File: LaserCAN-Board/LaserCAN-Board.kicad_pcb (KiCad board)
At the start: 4 copper layers, 25 x 25 mm, 35 parts, among them J2 TC2050-IDC-NL, U2 VL53L1CXV0FY1, U3 M24C64-RMN6TP, U4 STM32F103C8Tx, U5 MCP1703Ax-330xxTT, U6 SN65HVD230

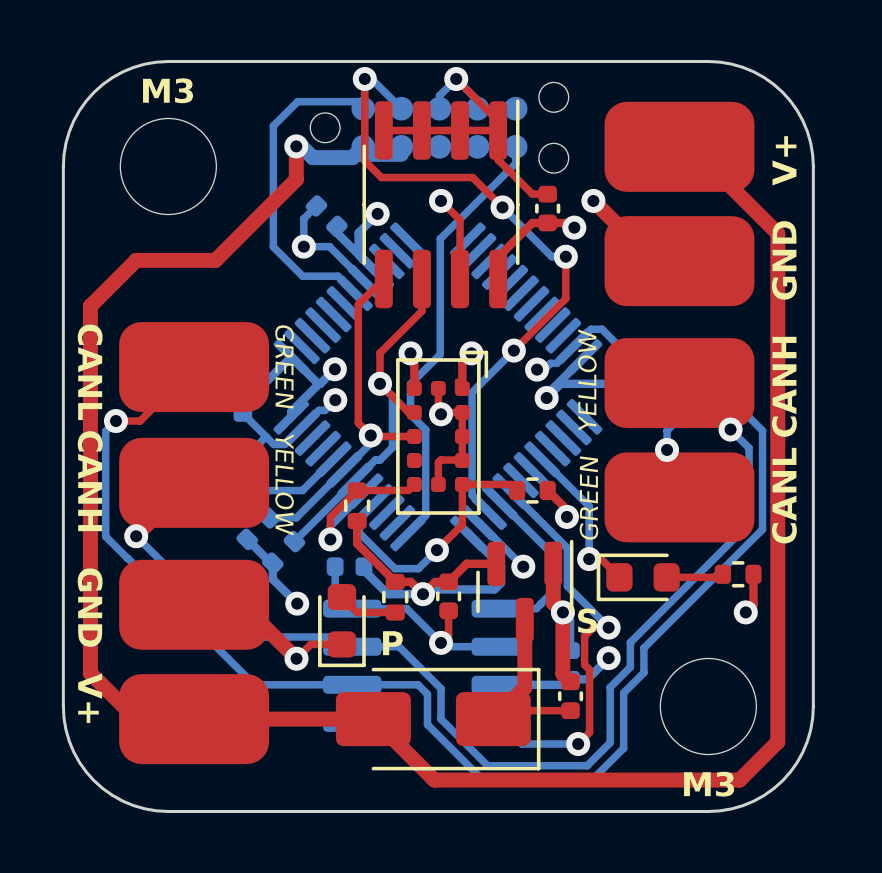
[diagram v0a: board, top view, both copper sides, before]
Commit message: Update to v3.1 - Improved voltage regulation performance, improved ESD protection
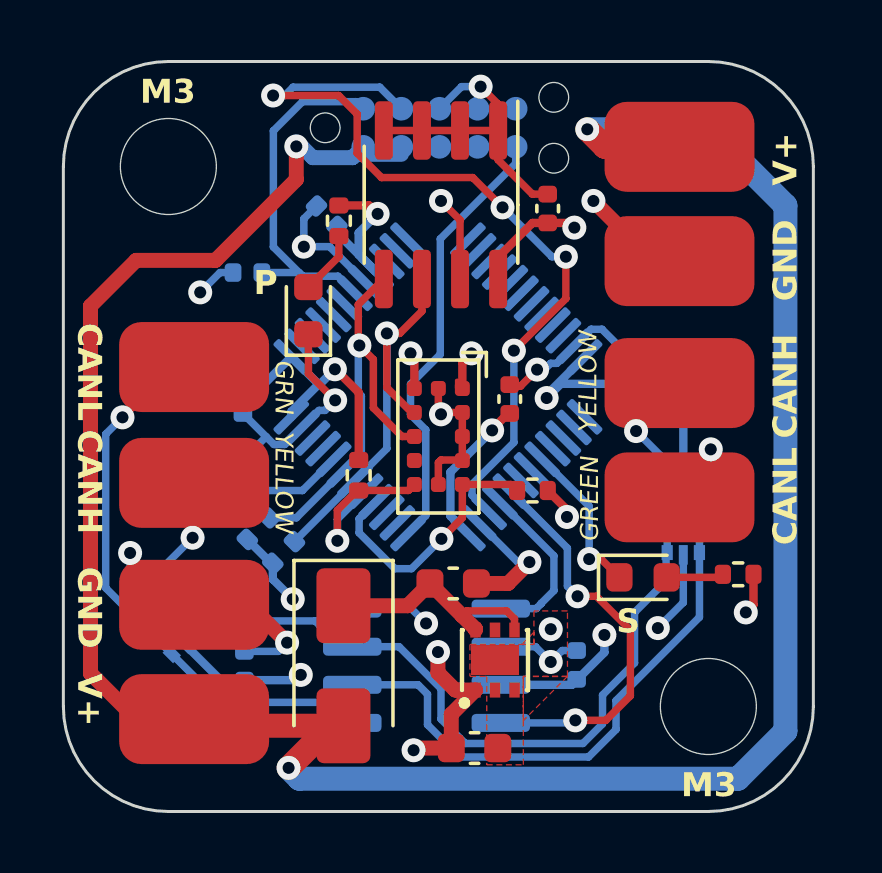
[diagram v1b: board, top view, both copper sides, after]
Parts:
- added C10: 100n, Capacitor_SMD:C_0402_1005Metric, B.Cu at (126.0, 120.1)
- added C11: 100n, Capacitor_SMD:C_0402_1005Metric, B.Cu at (140.6, 110.2)
- added C3: 10uF, Capacitor_SMD:C_0603_1608Metric, F.Cu at (133.7, 122.9)
- added U1: NCP730BMT330TBG, NCP730BMT330TBG:WDFN-6_L2.0-W2.0-P0.65-BL-EP-1, F.Cu at (134.4, 120.0)
- added U7: USBLC6-2P6, Package_TO_SOT_SMD:SOT-666, B.Cu at (140.7, 115.5)
- C1: value 1uF -> 10uF; footprint Capacitor_SMD:C_0402_1005Metric -> Capacitor_SMD:C_0603_1608Metric
- C4: value 1uF -> 100n; moved to B.Cu
- C8: moved to F.Cu
- U5: value MCP1703Ax-330xxTT -> USBLC6-2P6; footprint Package_TO_SOT_SMD:SOT-23 -> Package_TO_SOT_SMD:SOT-666; moved to B.Cu
- moved C4 12.7 mm to (126.1, 107.0), turned to 0 degrees
- moved R7 12.7 mm to (129.2, 105.3)
- moved U5 12.0 mm to (123.4, 118.8), turned to -45 degrees
- moved D3 10.4 mm to (128.2, 108.3)
- moved C8 7.73 mm to (134.9, 111.3), turned to 90 degrees
- moved C1 5.43 mm to (133.0, 117.4), turned to 0 degrees
- moved D1 3.48 mm to (129.3, 120.1), turned to -90 degrees
- moved R5 1.02 mm to (129.8, 113.8), turned to -90 degrees
- moved C9 0.20 mm to (137.1, 120.1)
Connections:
- C4 pad 1: +3V3 -> GND
- C4 pad 2: GND -> /NRST
- U5 pad 1: GND -> /CANL
- U5 pad 2: +3V3 -> GND
- U5 pad 3: Net-(D1-K) -> /CANH
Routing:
- net +3V3: track 44.7 -> 56.4 mm, vias 11 -> 14
- net +12V: track 72.3 -> 83.3 mm, vias 1 -> 3
- net /CANL: track 47.7 -> 42.5 mm
- net /SWDIO: track 22.4 -> 27.5 mm
- net GND: track 58.5 -> 62.4 mm, vias 11 -> 15
- net /I2C_SDA: track 11.9 -> 14.2 mm
- net /CANH: track 37.5 -> 35.4 mm
- net /I2C_SCL: track 12.5 -> 13.8 mm
- net /NRST: track 10.8 -> 12.1 mm
- net Net-(D1-K): track 6.42 -> 7.67 mm
- added copper zone on F.Cu, net GND
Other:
- board text added: "GRN"
- board text added: "LaserCAN Rev. 3.1"
- board text removed: "LaserCAN Rev. 3"

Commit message: Update to new power regulation circuitry
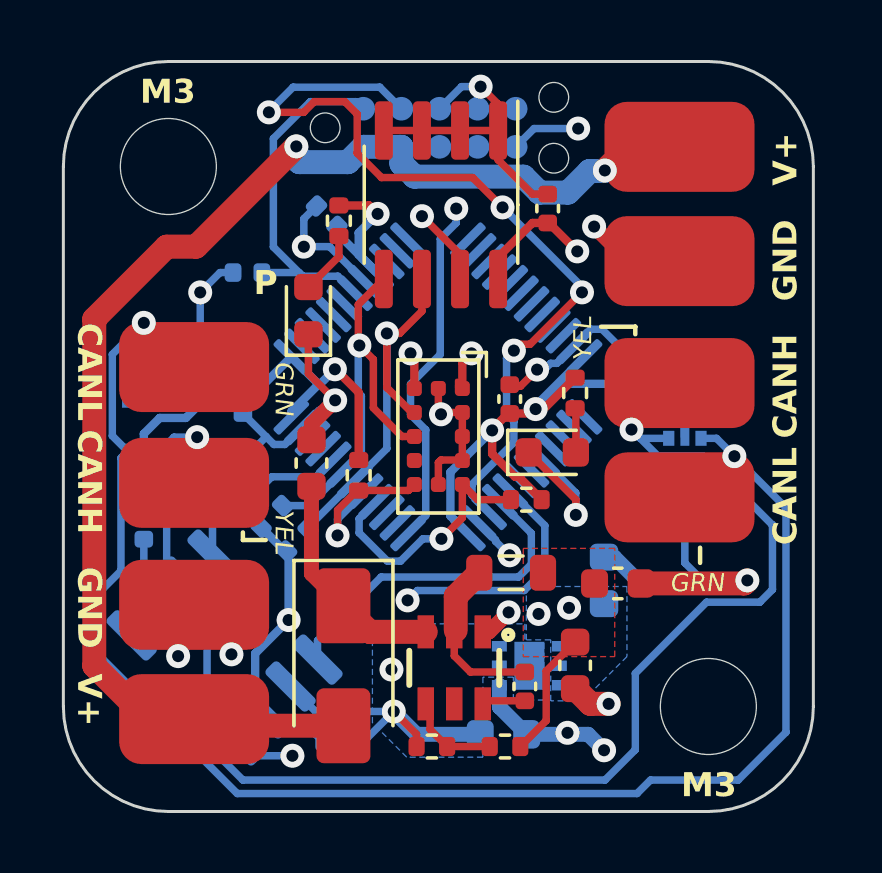
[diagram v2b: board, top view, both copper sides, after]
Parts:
- added C12: 10uF, Capacitor_SMD:C_0603_1608Metric, F.Cu at (128.3, 113.4)
- added C13: 10uF, Capacitor_SMD:C_0603_1608Metric, F.Cu at (138.5, 117.4)
- added C14: 100n, Capacitor_SMD:C_0402_1005Metric, F.Cu at (135.4, 120.8)
- added C15: 10uF, Capacitor_SMD:C_0603_1608Metric, F.Cu at (137.1, 120.1)
- added L1: 4.7uH, Inductor_SMD:L_0805_2012Metric, F.Cu at (134.9, 117.0)
- added R2: 41k 1%, Resistor_SMD:R_0402_1005Metric, F.Cu at (134.7, 122.8)
- added R8: 10k 1%, Resistor_SMD:R_0402_1005Metric, F.Cu at (132.3, 122.8)
- added U8: AP62200TWU-7, AP62200TWU-7:TSOT-26_L2.9-W1.6-P0.95-LS2.8-BL, F.Cu at (133.0, 120.2)
- C1, C3, U1: moved to B.Cu
- moved C9 8.35 mm to (129.2, 122.7), turned to 180 degrees
- moved R6 8.13 mm to (137.1, 111.0), turned to -90 degrees
- moved U6 6.76 mm to (125.4, 119.5), turned to 135 degrees
- moved U5 6.67 mm to (122.7, 112.1), turned to -90 degrees
- moved C10 5.77 mm to (122.7, 115.4), turned to -90 degrees
- moved D2 5.15 mm to (136.3, 113.0)
- moved C1 5.03 mm to (138.0, 117.3), turned to 90 degrees
- moved U7 2.11 mm to (140.7, 113.4)
- moved U1 1.16 mm to (135.5, 120.1), turned to 90 degrees
- moved C3 1.07 mm to (134.7, 122.4), turned to 180 degrees
- moved R3 0.61 mm to (127.8, 116.0)
- moved R4 0.61 mm to (126.9, 115.2)
- moved R1 0.37 mm to (135.4, 114.6)
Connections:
- C1 pad 1: Net-(D1-K) -> +3V9
- U1 pad 4: Net-(D1-K) -> +3V9
- U1 pad 6: Net-(D1-K) -> +3V9
- U5 pad 1: /CANL -> unconnected-(U5-I/O1-Pad1)
- U5 pad 3: /CANH -> unconnected-(U5-I/O2-Pad3)
- U7 pad 1: /CANL -> unconnected-(U7-I/O1-Pad1)
- U7 pad 3: /CANH -> unconnected-(U7-I/O2-Pad3)
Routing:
- net +12V: track 83.3 -> 44.8 mm, vias 3 -> 2
- net GND: track 62.4 -> 86.1 mm, vias 15 -> 16
- net /CANH: track 35.4 -> 45.2 mm
- net /CANL: track 42.5 -> 50.9 mm
- net +3V3: track 56.4 -> 62.7 mm, vias 14 -> 10
- net Net-(U8-SW): track 0.00 -> 5.62 mm
- net /CAN_TX: track 5.74 -> 11.3 mm
- net /SWCLK: track 14.8 -> 19.4 mm, vias 0 -> 2
- net +3V9: track 0.00 -> 4.24 mm, vias 0 -> 2
- net /CAN_RX: track 13.5 -> 17.0 mm
- net Net-(U8-FB): track 0.00 -> 3.14 mm
- net Net-(U8-BST): track 0.00 -> 1.44 mm
- net /SWDIO: track 27.5 -> 28.6 mm
- net /I2C_SDA: track 14.2 -> 13.6 mm
- net /I2C_SCL: track 13.8 -> 13.2 mm
- added copper zone on B.Cu, net +3V9
- added copper zone on F.Cu, net +3V9
- added copper zone on B.Cu, net GND
- removed copper zone on F.Cu, net GND
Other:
- board text added: "YEL"
- board text removed: "GREEN"
- board text removed: "S"
- board text removed: "YELLOW"

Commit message: Updates
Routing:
- net GND: track 86.1 -> 88.0 mm
- net +12V: track 44.8 -> 45.8 mm
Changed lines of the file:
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@@
     (fp_line (start -0.399622 0.56) (end 0.399622 0.56)
       (stroke (width 0.12) (type solid)) (layer "F.SilkS"))
-    (fp_line (start -1.75 -0.85) (end 1.75 -0.85)
+    (fp_line (start -1.75 -1) (end 1.75 -1)
       (stroke (width 0.05) (type solid)) (layer "F.CrtYd"))
-    (fp_line (start -1.75 0.85) (end -1.75 -0.85)
+    (fp_line (start -1.75 1) (end -1.75 -1)
       (stroke (width 0.05) (type solid)) (layer "F.CrtYd"))
-    (fp_line (start 1.75 -0.85) (end 1.75 0.85)
+    (fp_line (start 1.75 -1) (end 1.75 1)
       (stroke (width 0.05) (type solid)) (layer "F.CrtYd"))
-    (fp_line (start 1.75 0.85) (end -1.75 0.85)
+    (fp_line (start 1.75 1) (end -1.75 1)
       (stroke (width 0.05) (type solid)) (layer "F.CrtYd"))
     (fp_line (start -1 -0.45) (end 1 -0.45)
@@
     (fp_line (start 1 0.45) (end -1 0.45)
       (stroke (width 0.1) (type solid)) (layer "F.Fab"))
-    (pad "1" smd roundrect (at -1.0625 0) (size 0.875 1.2) (layers "F.Cu" "F.Paste" "F.Mask") (roundrect_rratio 0.25)
+    (pad "1" smd roundrect (at -1.0625 0) (size 0.875 1.7) (layers "F.Cu" "F.Paste" "F.Mask") (roundrect_rratio 0.25)
       (net 55 "Net-(U8-SW)") (pintype "passive"))
-    (pad "2" smd roundrect (at 1.0625 0) (size 0.875 1.2) (layers "F.Cu" "F.Paste" "F.Mask") (roundrect_rratio 0.25)
+    (pad "2" smd roundrect (at 1.0625 0) (size 0.875 1.7) (layers "F.Cu" "F.Paste" "F.Mask") (roundrect_rratio 0.25)
       (net 54 "+3V9") (pintype "passive"))
     (model "${KICAD6_3DMODEL_DIR}/Inductor_SMD.3dshapes/L_0805_2012Metric.wrl"
@@
   (segment (start 132.5 111.672) (end 132.588 111.76) (width 0.25) (layer "F.Cu") (net 1))
   (segment (start 133.3 111.7) (end 132.648 111.7) (width 0.25) (layer "F.Cu") (net 1))
-  (via (at 134.874 116.459) (size 0.8) (drill 0.4) (layers "F.Cu" "B.Cu") (net 1))
+  (via (at 134.8745 116.205) (size 0.8) (drill 0.4) (layers "F.Cu" "B.Cu") (net 1))
   (via (at 131.0132 121.666) (size 0.8) (drill 0.4) (layers "F.Cu" "B.Cu") (net 1))
   (via (at 131.953 105.156) (size 0.8) (drill 0.4) (layers "F.Cu" "B.Cu") (net 1))
@@
   (segment (start 142.748 117.348) (end 142.7988 117.2972) (width 0.5) (layer "B.Cu") (net 1))
   (segment (start 124.5616 108.7489) (end 124.5616 107.696) (width 0.25) (layer "B.Cu") (net 1))
-  (segment (start 134.40668 115.94786) (end 133.838742 115.379922) (width 0.25) (layer "B.Cu") (net 1))
-  (segment (start 134.40668 115.99168) (end 134.40668 115.94786) (width 0.25) (layer "B.Cu") (net 1))
+  (segment (start 134.841079 118.362267) (end 134.841079 119.448679) (width 0.5) (layer "B.Cu") (net 1))
   (segment (start 136.241359 110.061196) (end 136.452784 110.061196) (width 0.25) (layer "B.Cu") (net 1))
   (segment (start 124.971349 114.294651) (end 124.971349 116.435272) (width 0.25) (layer "B.Cu") (net 1))
   (segment (start 128.723363 111.630004) (end 128.520016 111.630004) (width 0.25) (layer "B.Cu") (net 1))
+  (segment (start 134.841079 119.448679) (end 135.5344 120.142) (width 0.5) (layer "B.Cu") (net 1))
   (segment (start 129.059265 111.294102) (end 128.723363 111.630004) (width 0.25) (layer "B.Cu") (net 1))
   (segment (start 122.682 116.854142) (end 122.682 115.923) (width 0.25) (layer "B.Cu") (net 1))
@@
   (segment (start 126.76 112.508) (end 125.984 111.732) (width 0.25) (layer "B.Cu") (net 1))
   (segment (start 125.984 113.282) (end 124.971349 114.294651) (width 0.25) (layer "B.Cu") (net 1))
-  (segment (start 134.874 116.459) (end 134.40668 115.99168) (width 0.25) (layer "B.Cu") (net 1))
+  (segment (start 134.40668 115.94786) (end 133.838742 115.379922) (width 0.25) (layer "B.Cu") (net 1))
+  (segment (start 134.61736 115.94786) (end 134.40668 115.94786) (width 0.25) (layer "B.Cu") (net 1))
   (segment (start 125.984 113.282) (end 125.986 113.282) (width 0.25) (layer "B.Cu") (net 1))
   (segment (start 140.716 116.713) (end 141.351 117.348) (width 0.25) (layer "B.Cu") (net 1))
@@
   (segment (start 133.8072 100.9396) (end 133.8072 101.5746) (width 0.25) (layer "B.Cu") (net 1))
   (segment (start 136.452784 110.061196) (end 137.020722 109.493258) (width 0.25) (layer "B.Cu") (net 1))
+  (segment (start 134.8745 116.205) (end 134.61736 115.94786) (width 0.25) (layer "B.Cu") (net 1))
   (segment (start 131.7752 122.428) (end 131.0132 121.666) (width 0.5) (layer "B.Cu") (net 1))
   (segment (start 125.986 113.282) (end 126.76 112.508) (width 0.25) (layer "B.Cu") (net 1))
@@
   (segment (start 136.583859 110.744) (end 139.22 110.744) (width 0.28) (layer "B.Cu") (net 2))
   (segment (start 122.682 113.066) (end 122.682 112.411) (width 0.28) (layer "B.Cu") (net 2))
-  (segment (start 138.8364 102.8446) (end 140.5382 102.8446) (width 0.8) (layer "F.Cu") (net 3))
   (segment (start 122.809 121.92) (end 124.3584 121.92) (width 0.8) (layer "F.Cu") (net 3))
+  (segment (start 138.8364 102.8446) (end 140.5382 102.8446) (width 0.8) (layer "F.Cu") (net 3))
   (segment (start 129.3368 122.142) (end 124.5804 122.142) (width 0.8) (layer "F.Cu") (net 3))
-  (segment (start 124.422164 106.172) (end 123.444 106.172) (width 0.8) (layer "F.Cu") (net 3))
-  (segment (start 127.764577 102.829587) (end 124.422164 106.172) (width 0.8) (layer "F.Cu") (net 3))
-  (segment (start 121.031 108.585) (end 121.031 120.142) (width 0.8) (layer "F.Cu") (net 3))
-  (segment (start 123.444 106.172) (end 121.031 108.585) (width 0.8) (layer "F.Cu") (net 3))
-  (segment (start 124.5804 122.142) (end 124.3584 121.92) (width 0.8) (layer "F.Cu") (net 3))
+  (segment (start 127.764577 104.137423) (end 125.73 106.172) (width 0.8) (layer "F.Cu") (net 3))
   (segment (start 121.031 120.142) (end 122.809 121.92) (width 0.8) (layer "F.Cu") (net 3))
+  (segment (start 121.031 108.204) (end 121.031 120.142) (width 0.8) (layer "F.Cu") (net 3))
+  (segment (start 125.73 106.172) (end 123.063 106.172) (width 0.8) (layer "F.Cu") (net 3))
+  (segment (start 123.063 106.172) (end 121.031 108.204) (width 0.8) (layer "F.Cu") (net 3))
+  (segment (start 124.5804 122.142) (end 124.3584 121.92) (width 0.8) (layer "F.Cu") (net 3))
   (segment (start 138.049 103.632) (end 138.8364 102.8446) (width 0.8) (layer "F.Cu") (net 3))
+  (segment (start 127.764577 102.829587) (end 127.764577 104.137423) (width 0.8) (layer "F.Cu") (net 3))
   (via (at 138.049 103.632) (size 0.8) (drill 0.4) (layers "F.Cu" "B.Cu") (net 3))
   (via (at 127.764577 102.829587) (size 0.8) (drill 0.4) (layers "F.Cu" "B.Cu") (net 3))
@@
   (segment (start 135.2316 122.8344) (end 136.0932 121.9728) (width 0.25) (layer "F.Cu") (net 54))
   (via (at 136.8552 118.2116) (size 0.8) (drill 0.4) (layers "F.Cu" "B.Cu") (net 54))
-  (via (at 135.8392 118.4148) (size 0.8) (drill 0.4) (layers "F.Cu" "B.Cu") (free) (net 54))
+  (via (at 135.89 118.491) (size 0.8) (drill 0.4) (layers "F.Cu" "B.Cu") (free) (net 54))
   (segment (start 133.08 117.8255) (end 133.08 118.962) (width 0.8) (layer "F.Cu") (net 55))
   (segment (start 133.03 119.012) (end 133.03 119.812) (width 0.25) (layer "F.Cu") (net 55))
